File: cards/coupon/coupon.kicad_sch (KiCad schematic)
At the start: 65 parts, among them J1 IN N1 N2 N3, J2 BUS, Q1 2N7000, Q10 2N7000, Q11 2N7000, Q12 2N7000, Q13 2N7000, Q14 2N7000, Q15 2N7000, Q16 2N7000, Q17 2N7000, Q18 2N7000, Q19 2N7000, Q2 2N7000, Q20 2N7000, Q21 2N7000, Q22 2N7000, Q23 2N7000, Q24 2N7000, Q25 2N7000, Q26 2N7000, Q3 2N7000, Q4 2N7000, Q5 2N7000, Q6 2N7000, Q7 2N7000, Q8 2N7000, Q9 2N7000

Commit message: Coupon respun with every cell on it (D056): the bench's expected readings from its own netlist
The coupon is what proves the simulations right before the second order, and
the old one measured only the inverter. It now carries, each with a test
loop: the 5-inverter ring (a buffered loop and a raw one on the ring node),
fan-out 1 and 10, NAND3 and NOR3, the bus driver against 10k, the clock
card's oscillator (its Schmitt pair and 100k + 47 nF, the same parts drawn
on the sheet), a master-slave flip-flop wired as a toggle with the
asynchronous reset the counters and the sequencer use, the D053 line
driver (1k inverter, 100 ohm, diode, 10k pull-down; 3.3 nF clipped on at
the bench), a diode-connected transistor on 4.7k that reads its own
threshold, and a program row (3.3k, 1N4148, 220k). Inputs IN N1 N2 N3 RST
on a 6-pin header with 1 Meg pull-downs, power on a 2-pin header for the
bench supply, fifteen loops. 57 transistors on six tile columns of one
100 x 100 card; ERC 0, one freerouting pass, DRC 0 errors (one dangling
trunk end), 0 open under JLCPCB's minimum rules too.

sim/tb_coupon.py simulates the routed card's kicad export (or the gate list
plus the sheet parts, which agree at every uniform corner) at TYP, LO, HI
and MIX seeds 1..3, a x10 probe on every loop, and writes the bands the
bench must land in: sim/results/coupon_expected.md. Ring 5.9 to 23.6 us
(14.6 typical), fan-out-1 rise 10 to 12 us, fan-out-10 rise 67 to 77 us,
stacks under 2 mV, Schmitt hysteresis 0.4 V about the threshold,
oscillator 1.64 to 2.55 ms, Q at half that with one edge per clock edge,
DRV 4.0 V high, 6.6 us up and 49 us down into 3.3 nF, VTO 0.88 to 3.02 V,
ROM 4.52 V, 5 to 8 mA with IN low and 11 to 14 mA with IN high.

Two things the testbench found before the copper did: with low-threshold
transistors the ring swings only to 1.6 to 3 V and a high-threshold buffer
never switches (the buffered loop was blind at two MIX seeds; hence the
raw RING0 loop), and while RST holds the flip-f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
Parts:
- removed J1: IN N1 N2 N3, Connector_PinHeader_2.54mm:PinHeader_1x04_P2.54mm_Vertical, symbol Connector_Generic:Conn_01x04
- removed J2: BUS, Connector_IDC:IDC-Header_2x32_P2.54mm_Vertical, symbol Connector_Generic:Conn_02x32_Odd_Even
- added C3: 47n, Capacitor_THT:C_Disc_D5.0mm_W2.5mm_P2.50mm, symbol Device:C
- added D2, D3: 1N4148, Diode_THT:D_DO-35_SOD27_P7.62mm_Horizontal, symbol Device:D
- added J1: IN N1 N2 N3 RST GND, Connector_PinHeader_2.54mm:PinHeader_1x06_P2.54mm_Vertical, symbol Connector_Generic:Conn_01x06
- added J2: +5V GND, Connector_PinHeader_2.54mm:PinHeader_1x02_P2.54mm_Vertical, symbol Connector_Generic:Conn_01x02
- added J3: BUS, Connector_IDC:IDC-Header_2x32_P2.54mm_Vertical, symbol Connector_Generic:Conn_02x32_Odd_Even
- added Q27, Q28, Q29, Q30, Q31, Q32, Q33, Q34, Q35, Q36, Q37, Q38, Q39, Q40, Q41, Q42, Q43, Q44, Q45, Q46, Q47, Q48, Q49, Q50, Q51, Q52, Q53, Q54, Q55, Q56, Q57: 2N7000, Package_TO_SOT_THT:TO-92_Inline_Wide, symbol Transistor_FET:2N7000
- added R27, R28, R29, R30, R31, R32, R33, R34, R35, R36, R37, R47: 47k, Resistor_THT:R_Axial_DIN0207_L6.3mm_D2.5mm_P5.08mm_Vertical, symbol Device:R
- added R38, R41, R49: 1k, Resistor_THT:R_Axial_DIN0207_L6.3mm_D2.5mm_P5.08mm_Vertical, symbol Device:R
- added R39: 4.7k, Resistor_THT:R_Axial_DIN0207_L6.3mm_D2.5mm_P5.08mm_Vertical, symbol Device:R
- added R40: 3.3k, Resistor_THT:R_Axial_DIN0207_L6.3mm_D2.5mm_P5.08mm_Vertical, symbol Device:R
- added R42, R43, R44, R45, R46: 1Meg, Resistor_THT:R_Axial_DIN0207_L6.3mm_D2.5mm_P5.08mm_Vertical, symbol Device:R
- added R48, R52: 10k, Resistor_THT:R_Axial_DIN0207_L6.3mm_D2.5mm_P5.08mm_Vertical, symbol Device:R
- added R50: 100k, Resistor_THT:R_Axial_DIN0207_L6.3mm_D2.5mm_P5.08mm_Vertical, symbol Device:R
- added R51: 100, Resistor_THT:R_Axial_DIN0207_L6.3mm_D2.5mm_P5.08mm_Vertical, symbol Device:R
- added R53: 220k, Resistor_THT:R_Axial_DIN0207_L6.3mm_D2.5mm_P5.08mm_Vertical, symbol Device:R
- added TP10: TP_OSC, TestPoint:TestPoint_Loop_D2.50mm_Drill1.0mm, symbol Connector:TestPoint
- added TP11: TP_Q, TestPoint:TestPoint_Loop_D2.50mm_Drill1.0mm, symbol Connector:TestPoint
- added TP12: TP_DRV, TestPoint:TestPoint_Loop_D2.50mm_Drill1.0mm, symbol Connector:TestPoint
- added TP13: TP_ROM, TestPoint:TestPoint_Loop_D2.50mm_Drill1.0mm, symbol Connector:TestPoint
- added TP14: GND, TestPoint:TestPoint_Loop_D2.50mm_Drill1.0mm, symbol Connector:TestPoint
- added TP15: +5V, TestPoint:TestPoint_Loop_D2.50mm_Drill1.0mm, symbol Connector:TestPoint
- added TP7: TP_BUS, TestPoint:TestPoint_Loop_D2.50mm_Drill1.0mm, symbol Connector:TestPoint
- added TP8: TP_VTO, TestPoint:TestPoint_Loop_D2.50mm_Drill1.0mm, symbol Connector:TestPoint
- added TP9: X, TestPoint:TestPoint_Loop_D2.50mm_Drill1.0mm, symbol Connector:TestPoint
- R1: value 1Meg -> 10k
- R2, R3, R4: value 1Meg -> 47k
- R22: value 47k -> 4.7k
- R26: value 1k -> 47k
- R5: value 10k -> 47k
- TP2: value TP_FO1 -> RING0
- TP3: value TP_FO10 -> TP_FO1
- TP4: value TP_NAND -> TP_FO10
- TP5: value TP_NOR -> TP_NAND
- TP6: value TP_BUS -> TP_NOR
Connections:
- net +5V: now also R1.1, R10.2, R11.1, R15.1, R16.2, R17.1, R2.2, R21.1, R24.1, R25.2, R26.1, R3.1, R4.2, R9.1, J2.1 (Pin_1), J3.1 (Pin_1), J3.2 (Pin_2), J3.63 (Pin_63), R27.2, R28.1, R29.2, R30.1, R31.2, R32.2, R33.1, R34.1, R35.2, R36.2, R37.1, R38.1, R39.2, R40.1, R41.1, R47.1, R48.1, TP15.1; no longer R10.1, R11.2, R15.2, R16.1, R17.2, R21.2, R24.2, R25.1, R26.2, R9.2
- net GND: now also C3.2, J1.6 (Pin_6), J2.2 (Pin_2), J3.3 (Pin_3), J3.4 (Pin_4), J3.6 (Pin_6), J3.64 (Pin_64), J3.8 (Pin_8), Q27.1 (S), Q28.1 (S), Q29.1 (S), Q30.1 (S), Q31.1 (S), Q33.1 (S), Q35.1 (S), Q37.1 (S), Q40.1 (S), Q41.1 (S), Q43.1 (S), Q45.1 (S), Q47.1 (S), Q50.1 (S), Q51.1 (S), Q52.1 (S), Q53.1 (S), Q54.1 (S), Q55.1 (S), R42.1, R43.2, R44.1, R45.2, R46.1, R49.2, R52.2, R53.2, TP14.1; no longer R1.2, R2.2, R3.2, R4.2
- net IN: now also J1.1 (Pin_1), Q54.2 (G), Q55.2 (G), R42.2; no longer Q26.2 (G), R1.1
- net LOAD0: now also R10.1; no longer R14.1
- net LOAD1: now also R11.2; no longer R15.1
- net LOAD2: now also R12.1; no longer R16.2
- net LOAD3: now also R13.2; no longer R17.1
- net LOAD4: now also R14.1; no longer R18.1
- net LOAD5: now also R15.2; no longer R19.2
- net LOAD6: now also R16.1; no longer R20.1
- net LOAD7: now also R17.2; no longer R21.1
- net LOAD8: now also R18.1; no longer R22.2
- net LOAD9: now also R19.2; no longer R23.1
- net N1: now also J1.2 (Pin_2), R43.1; no longer R2.1
- net N2: now also J1.3 (Pin_3), R44.2; no longer R3.1
- net N3: now also J1.4 (Pin_4), R45.1; no longer R4.1
- net RING0: now also R6.1, TP2.1; no longer R10.2
- net RING1: now also R2.1; no longer R6.1
- net RING2: now also R3.2; no longer R7.2
- net RING3: now also R4.1; no longer R8.1
- net RING4: now also R5.2; no longer R9.1
- net TP_BUS: now also R1.2, TP7.1; no longer R5.2, TP6.1
- net TP_FO1: now also R8.1, TP3.1; no longer R12.1, TP2.1
- net TP_FO10: now also R9.2, TP4.1; no longer R13.2, TP3.1
- net TP_NAND: now also R20.1, TP5.1; no longer R24.1, TP4.1
- net TP_NOR: now also R21.2, TP6.1; no longer R25.2, TP5.1
- net TP_RING: now also R7.2; no longer R11.1
- net at D1.1 (K): now also Q55.3 (D); no longer Q26.3 (D)
- net at D1.2 (A): now also R41.2; no longer R26.1
- new net: Q32.1 (S), Q33.3 (D)
- new net: Q36.1 (S), Q37.3 (D)
- new net: Q49.1 (S), Q50.3 (D)
- new net: Q48.1 (S), Q49.3 (D)
- new net: Q38.1 (S), Q39.3 (D)
- new net: Q56.3 (D), Q57.2 (G), R47.2
- new net: Q39.1 (S), Q40.3 (D)
- new net: Q46.1 (S), Q47.3 (D)
- new net: D2.2 (A), R51.2
- new net: Q34.1 (S), Q35.3 (D)
- new net: Q42.1 (S), Q43.3 (D)
- new net: Q44.1 (S), Q45.3 (D)
- new net DRVN: Q52.3 (D), R38.2, R51.1
- new net QN: Q31.2 (G), Q32.2 (G), Q51.3 (D), R37.2
- new net ROW: D3.2 (A), Q54.3 (D), R40.2
- new net RST: J1.5 (Pin_5), Q28.2 (G), R46.2
- new net RSTN: Q28.3 (D), Q40.2 (G), Q50.2 (G), R24.2
- new net SA: Q26.3 (D), Q27.2 (G), R22.2, R50.1
- new net TP_DRV: D2.1 (K), R52.1, TP12.1
- new net TP_OSC: Q27.3 (D), Q29.2 (G), Q52.2 (G), R23.1, TP10.1
- new net TP_Q: Q46.3 (D), Q48.2 (G), Q51.2 (G), R35.1, TP11.1
- new net TP_Q_ckb: Q30.3 (D), Q43.2 (G), Q44.2 (G), R26.2
- new net TP_Q_ckn: Q29.3 (D), Q30.2 (G), Q33.2 (G), Q34.2 (G), R25.1
- new net TP_Q_dn: Q31.3 (D), Q35.2 (G), R27.1
- new net TP_Q_m1: Q32.3 (D), Q36.2 (G), R28.2
- new net TP_Q_m2: Q34.3 (D), Q39.2 (G), R29.1
- new net TP_Q_mq: Q36.3 (D), Q38.2 (G), Q41.2 (G), Q42.2 (G), R30.2
- new net TP_Q_mqi: Q41.3 (D), Q45.2 (G), R32.1
- new net TP_Q_mqn: Q37.2 (G), Q38.3 (D), R31.1
- new net TP_Q_qn: Q47.2 (G), Q48.3 (D), R36.1
- new net TP_Q_sa: Q42.3 (D), Q46.2 (G), R33.2
- new net TP_Q_sb: Q44.3 (D), Q49.2 (G), R34.2
- new net TP_ROM: D3.1 (K), R53.1, TP13.1
- new net TP_VTO: Q53.2 (G), Q53.3 (D), R39.1, TP8.1
- new net VD2: Q26.2 (G), Q57.3 (D), R48.2
- new net VS: Q56.1 (S), Q57.1 (S), R49.1
- new net X: C3.1, Q56.2 (G), R50.2, TP9.1
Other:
- note added: "57 transistors, 100 x 100 mm (docs/cards.md). Power: 5 V on the 2-pin header from the bench supply (limit 300 mA), or the bus header (the hub; no other bus line is used). Drive IN, N1, N2, N3, RST from the 6-pin header (each has a 1Meg pull-down, so open = 0; RST open lets the flip-flop run). Measure at the test loops: RING period (gate delay = period / 10; RING0 is the ring node itself, for when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"
- note added: "Bench supply in, 5.0 V, current limit 300 mA"
- note added: "LINE DRIVER (D053): DRVN (1k pull-up) through 100 ohm and a diode into TP_DRV with a 10k pull-down, as the clock card drives CLK and RST and the panel its buttons. Clip 3.3 nF from TP_DRV to GND: the ribbon and the cards' gates."
- note added: "LINE DRIVER (D053): DRVN = NOT SB with a 1k pull-up, through 100 ohm and a diode (drawn below) into TP_DRV with a 10k pull-down. Clip 3.3 nF on TP_DRV: the CLK edge every card sees."
- note added: "NIBBLE CARD COUPON: every cell of the machine in copper, measured before any card is trusted"
- note added: "OSCILLATOR BUFFERS (the clock card's): SA = NOT VD2 (VD2 is the Schmitt pair's output, drawn below) with a 4.7k pull-up drives 100k back to X; SB = NOT SA is the clock, TP_OSC."
- note added: "PROGRAM ROW: ROW (3.3k pull-up) through a 1N4148 into TP_ROM with the hub's 220k pull-down (D048): the M line's high is 5 V less a diode drop."
- note added: "PROGRAM ROW: ROW = NOT IN with a 3.3k pull-up, through a 1N4148 (drawn below) into TP_ROM with the hub's 220k pull-down. TP_ROM high = 5 V less a diode."
- note added: "RING OSCILLATOR: 5 inverters in a loop, buffered to TP_RING. Period = 10 gate delays."
- note added: "SCHMITT TRIGGER (the clock card's, cards/clock): Q1 (gate X) and Q2 (gate = Q1's drain) share RS = 1k. Q2 on: source at 0.45 V (RD2 10k); Q1 on: source at 0.1 V (RD1 47k). VD2, Q2's drain, is the output: 0.5 V with X low, 5 V with X high."
- note added: "TEST LOOPS"
- note added: "THRESHOLD: gate tied to drain, 4.7k pull-up. TP_VTO settles about 0.1 V above this transistor's threshold (0.6 mA)."
- note added: "TIMING: SA -> 100k -> X, 47n from X to GND: the clock card at its fastest setting (its pot at zero), about 500 Hz. X swings only between the two trip points, about half a volt around Vth."
- note added: "TOGGLE FLIP-FLOP: the NAND master-slave D flip-flop (nmos.ff) with D = NOT Q, clocked by SB, reset by RSTN = NOT RST. TP_Q runs at half the oscillator rate while RST is low; RST high holds it at 0."
- note removed: "26 transistors, 100 x 100 mm (docs/cards.md). Power from the bus header (the hub, or 5 V on pins 1-2 and ground on 3-4; no other bus line is used). Drive IN, N1, N2, N3 from the 4-pin header (each has a 1Meg pull-down, so open = 0). Measure at the test loops: TP_RING period (gate delay = period / 10), TP_FO1 vs TP_FO10 rise time (fan-out 1 vs 10), TP_NAND / TP_NOR output low with all three inputs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"
- note removed: "NIBBLE CARD COUPON: the 2N7000 + 47k cell in copper, measured before any card is trusted"
- note removed: "RING OSCILLATOR: 5 inverters in a loop, buffered to TP_RING. Period = 10 gate delays (simulated 12 us)."

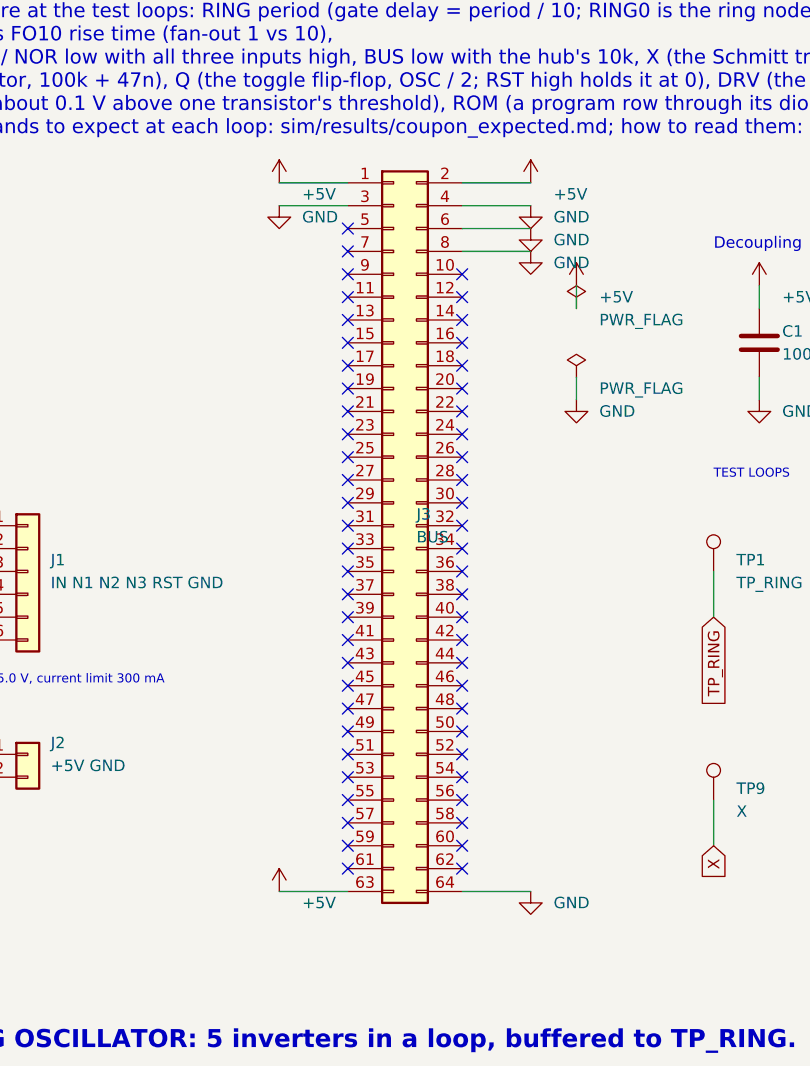
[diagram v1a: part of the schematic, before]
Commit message: The bus headers go on the back of all 26 boards, no track moved; the silkscreen refitted (D059, D062)
An IDC socket lies across its ribbon, so the ribbon could never run along a
row of cards as drawn. It runs behind them, and the 64-pin headers are
soldered on the back. This commit is that move, made in place on the routed
boards: no board was routed again.

How the header sits (D062): in the holes it had, turned over top to bottom,
notch toward the top edge. A pin of the odd row is then in the hole its even
neighbour had, so the two signals of every pair of pins change places: CLK
is pin 6, RST pin 8, +5V pins 1, 2 and 64. bus.py keeps both tables: PINS,
what the header's pins carry, and HOLES, what the copper was routed to.

The proof, on all 26 boards against 992a90f (sim/board_diff.py):
  netlist the same, element for element; every track, every via and every
  hole the same; each copper and mask layer differs by two pad shapes per
  header (pin 1's square went to the hole beside it, both on +5V) and the
  ground pour's outline round those two pads, nowhere else by more than a
  tenth of a micrometre.
sim/rebuild_check.py runs every builder into a scratch directory: each
writes the plan and the netlist that are committed, so a rebuild gives
this board. order_check.py --machine holds every pad of the 27 headers to
bus.py and requires them on the back.

What the move costs: on the ribbon RST had a ground conductor on both
sides; now one neighbour is BUS1#. tb_rst_neighbour.py puts the two lines
on the bench with every gate the routed boards hang on them: RST rises
0.28 to 0.43 V when BUS1# is released, against a lowest threshold of 0.8 V
(sim/results/rst_neighbour.md). The machine deck's crosstalk option now
couples the pins that are neighbours on the ribbon; the crosstalk stage of
the machine gate has to be run again on that order.

Silkscreen (pcb.fit_silk): every label to 1.0 mm where it has room, off
pads, vias, outlines and other labels, out from under the pa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
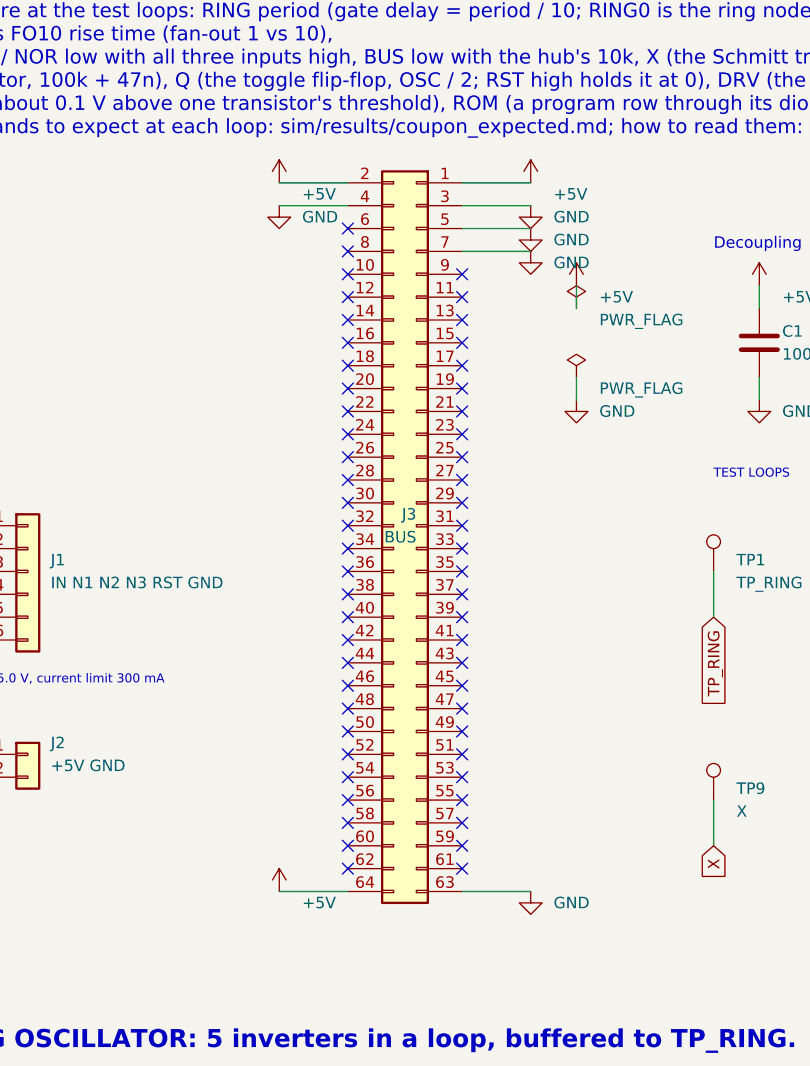
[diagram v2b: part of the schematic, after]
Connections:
- net +5V: now also J3.64 (Pin_64); no longer J3.63 (Pin_63)
- net GND: now also J3.5 (Pin_5), J3.63 (Pin_63), J3.7 (Pin_7); no longer J3.6 (Pin_6), J3.64 (Pin_64), J3.8 (Pin_8)
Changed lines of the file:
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@@
 	(symbol
 		(lib_id "Connector_Generic:Conn_02x32_Odd_Even")
-		(at 76.2 86.36 0)
+		(at 78.74 86.36 0)
+		(mirror y)
 		(unit 1)
 		(body_style 1)
